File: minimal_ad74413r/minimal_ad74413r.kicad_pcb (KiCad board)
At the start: 4 copper layers, 55.9 x 39.4 mm, 101 parts, among them J1 FW-02-03-G-D-085-315, J2 FW-02-03-G-D-085-315, J3 FW-04-03-G-D-085-315, J4 FW-04-03-G-D-085-315, J5 FW-02-03-G-D-085-315, J6 FW-02-03-G-D-085-315, J7 FW-14-03-G-D-085-155, Q1 ZXMP6A17E6TA, Q2 ZXMP6A17E6TA, Q3 ZXMP6A17E6TA, Q4 ZXMP6A17E6TA, U1 AD74413RBCPZ

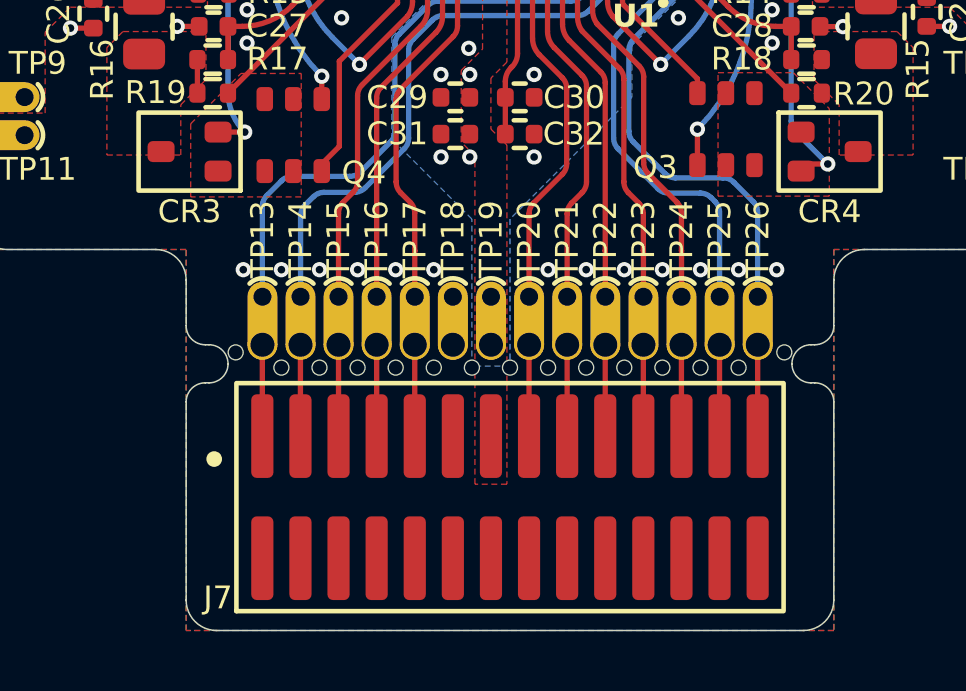
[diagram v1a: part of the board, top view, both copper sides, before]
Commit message: Update subproject commit and add new configuration and library entries for KiCAD_Symbol_Generator
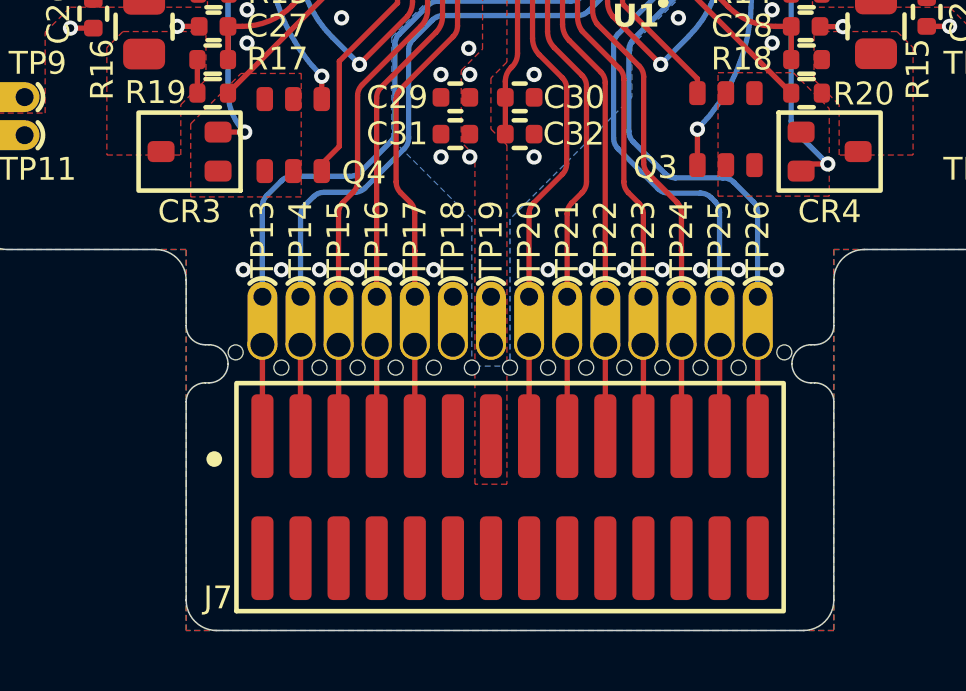
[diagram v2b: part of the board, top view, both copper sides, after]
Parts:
- removed REF** (x6): mouse-bite-midle-50mil-200mil, mouse_bite_footprints:mouse-bite-midle-50mil-200mil
- removed REF**: mouse-bite-50mil-790mil, mouse_bite_footprints:mouse-bite-50mil-790mil
- added MB1: mouse-bite-midle-50mil-200mil, mouse_bite_footprints:mouse-bite-midle-50mil-200mil, F.Cu at (170.2, 111.8)
- added MB2: mouse-bite-midle-50mil-200mil, mouse_bite_footprints:mouse-bite-midle-50mil-200mil, F.Cu at (170.2, 101.6)
- added MB3: mouse-bite-midle-50mil-200mil, mouse_bite_footprints:mouse-bite-midle-50mil-200mil, F.Cu at (170.2, 94.0)
- added MB4: mouse-bite-midle-50mil-200mil, mouse_bite_footprints:mouse-bite-midle-50mil-200mil, F.Cu at (133.3, 94.0)
- added MB5: mouse-bite-midle-50mil-200mil, mouse_bite_footprints:mouse-bite-midle-50mil-200mil, F.Cu at (133.3, 101.6)
- added MB6: mouse-bite-midle-50mil-200mil, mouse_bite_footprints:mouse-bite-midle-50mil-200mil, F.Cu at (133.3, 111.8)
- added MB7: mouse-bite-midle-50mil-200mil, mouse_bite_footprints:mouse-bite-50mil-790mil, F.Cu at (151.8, 119.9)

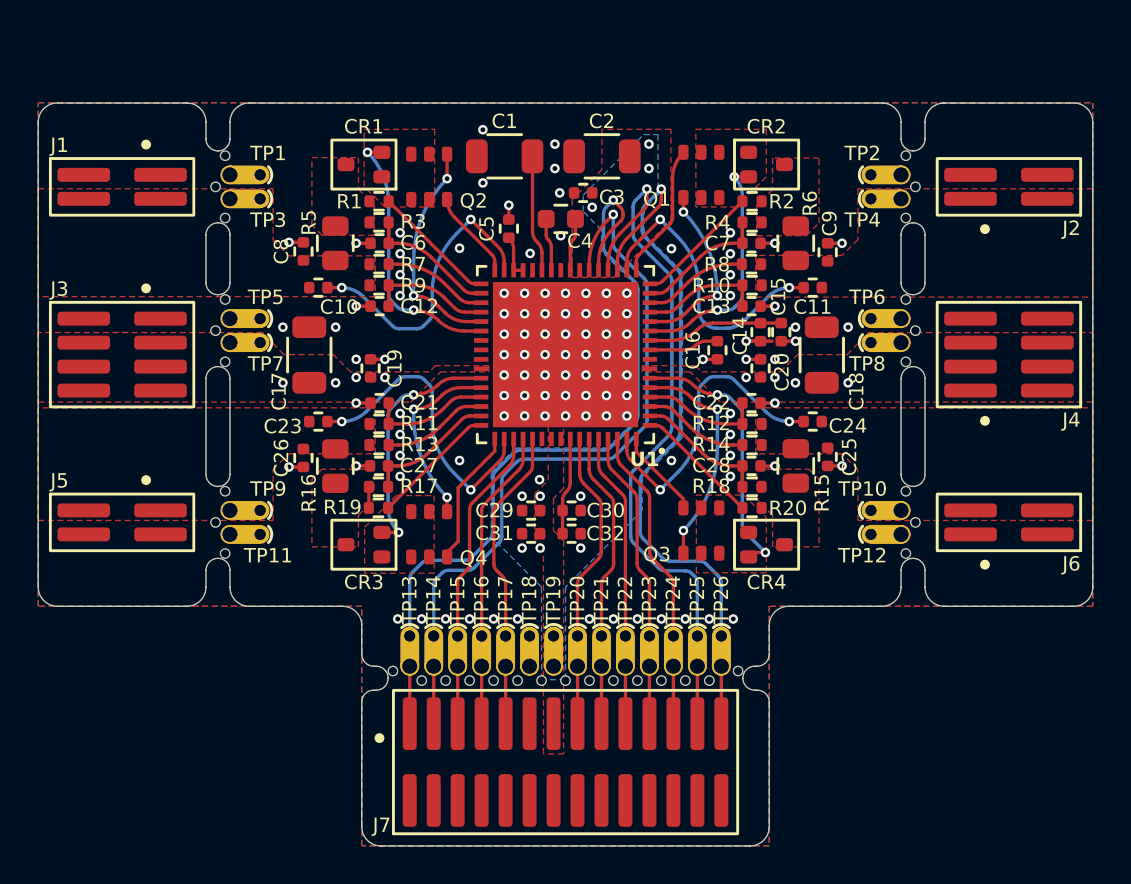
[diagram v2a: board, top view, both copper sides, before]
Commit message: Update subproject commit and add new library entries for KiCAD_Symbol_Generator
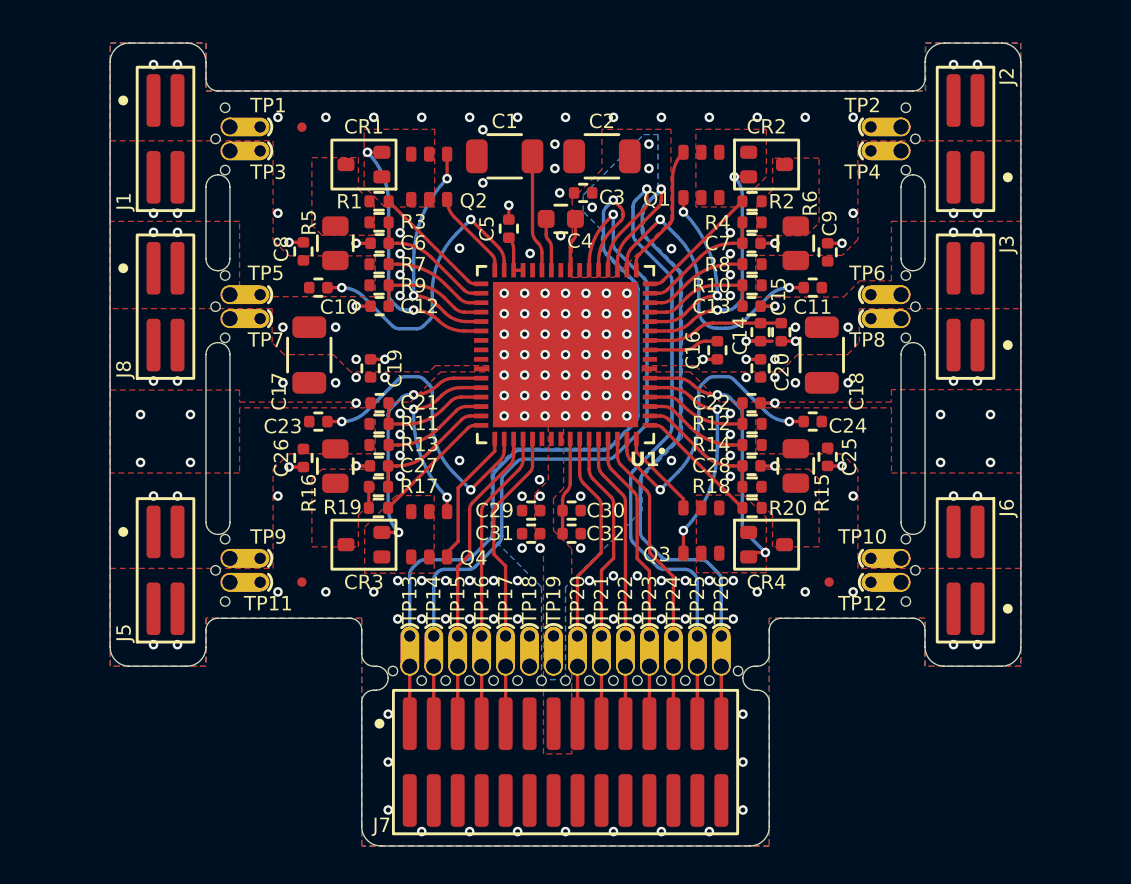
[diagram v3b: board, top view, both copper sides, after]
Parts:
- removed J4: FW-04-03-G-D-085-315, connector_footprints:FW-04-03-G-D-085-315
- added FID1: Fiducial, no_components_footprints:Fiducial_0.5mm_Mask1mm, F.Cu at (137.8, 90.8)
- added FID2: Fiducial, no_components_footprints:Fiducial_0.5mm_Mask1mm, F.Cu at (137.8, 114.9)
- added FID3: Fiducial, no_components_footprints:Fiducial_0.5mm_Mask1mm, F.Cu at (165.7, 114.9)
- added J8: FW-02-03-G-D-085-315, connector_footprints:FW-02-03-G-D-085-315, F.Cu at (130.6, 100.3)
- J3: value FW-04-03-G-D-085-315 -> FW-02-03-G-D-085-315; footprint connector_footprints:FW-04-03-G-D-085-315 -> connector_footprints:FW-02-03-G-D-085-315
- moved J3 44.8 mm to (173.0, 100.3), turned to 180 degrees
- moved J2 3.43 mm to (173.0, 91.4), turned to 180 degrees
- moved J6 3.43 mm to (173.0, 114.3), turned to 180 degrees
- moved J1 3.43 mm to (130.6, 91.4), turned to 0 degrees
- moved J5 3.43 mm to (130.6, 114.3), turned to 0 degrees
- moved MB3 2.54 mm to (170.2, 91.4)
- moved MB4 2.54 mm to (133.3, 91.4)
- moved TP10 2.54 mm to (169.5, 113.7)
- moved TP3 2.54 mm to (134.0, 92.1)
- moved TP4 2.54 mm to (169.5, 92.1)
- moved TP9 2.54 mm to (134.0, 113.7)
- moved MB1 2.54 mm to (170.2, 114.3)
- moved MB6 2.54 mm to (133.3, 114.3)
- moved TP1 2.54 mm to (134.0, 90.8)
- moved TP11 2.54 mm to (134.0, 114.9)
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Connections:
- J1 pad 2: GNDA -> /CHANNEL_3
- J1 pad 3: /CHANNEL_3 -> GNDA
- J2 pad 2: /CHANNEL_2 -> GNDA
- J2 pad 3: GNDA -> /CHANNEL_2
- J3 pad 1: GNDA -> /VDD_24V
- J3 pad 4: /VDD_24V -> GNDA
- J5 pad 2: /CHANNEL_4 -> GNDA
- J5 pad 3: GNDA -> /CHANNEL_4
- J6 pad 2: GNDA -> /CHANNEL_1
- J6 pad 3: /CHANNEL_1 -> GNDA
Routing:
- net GNDA: track 14.8 -> 14.0 mm, vias 118 -> 187
- net /VDD_24V: vias 8 -> 12
- net /CHANNEL_4: vias 0 -> 2
- net /CHANNEL_3: vias 0 -> 2
- net /CHANNEL_2: vias 0 -> 2
- net /CHANNEL_1: vias 0 -> 2
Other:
- board size 55.9 x 39.4 mm -> 48.3 x 42.5 mm

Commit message: Update project files and enhance structure
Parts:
- J3, J8: value FW-02-03-G-D-085-315 -> FW-02-03-G-D-085-155; footprint connector_footprints:FW-02-03-G-D-085-315 -> connector_footprints:FW-02-03-G-D-085-155
- moved J2 0.39 mm to (173.4, 91.4)
- moved J3 0.39 mm to (173.4, 100.3)
- moved J6 0.39 mm to (173.4, 114.3)
- moved J1 0.39 mm to (130.2, 91.4)
- moved J5 0.39 mm to (130.2, 114.3)
- moved J8 0.39 mm to (130.2, 100.3)
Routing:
- net GNDA: vias 187 -> 191

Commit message: Update reference properties in minimal_ad74413r schematic
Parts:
- renumbered J8 to J3, J3 to J4, MB4 to MB1, MB3 to MB2, MB5 to MB3, MB2 to MB4, MB6 to MB5, MB1 to MB6
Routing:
- net /CHANNEL_4: vias 2 -> 0
- net /CHANNEL_3: vias 2 -> 0
- net /CHANNEL_2: vias 2 -> 0
- net /CHANNEL_1: vias 2 -> 0

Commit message: Backup
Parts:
- J1, J2, J5, J6: value FW-02-03-G-D-085-315 -> FW-02-03-G-D-085-155; footprint connector_footprints:FW-02-03-G-D-085-315 -> connector_footprints:FW-02-03-G-D-085-155
